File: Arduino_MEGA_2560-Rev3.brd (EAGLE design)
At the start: 111.3 x 99 mm, 32 parts

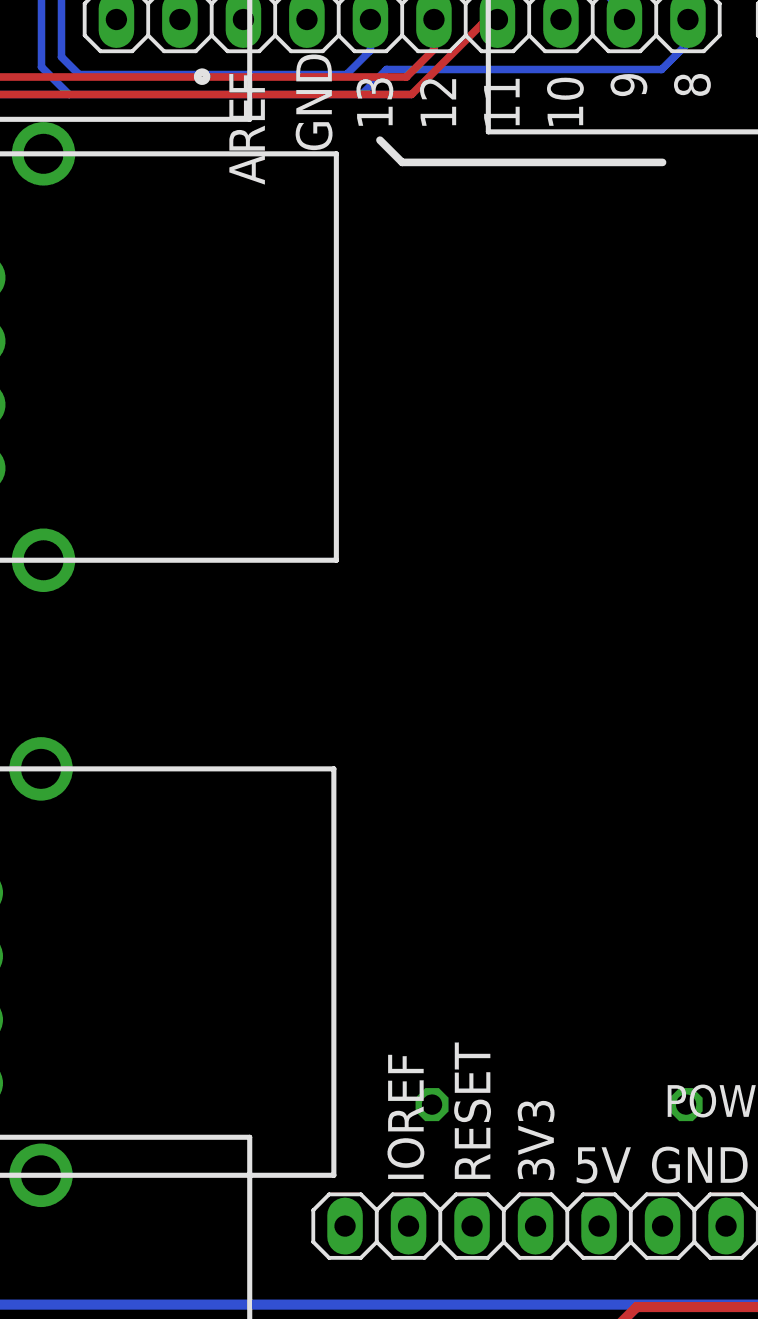
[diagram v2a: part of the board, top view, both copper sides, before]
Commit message: nuevas resistencias, revisar los pines de entrada salida
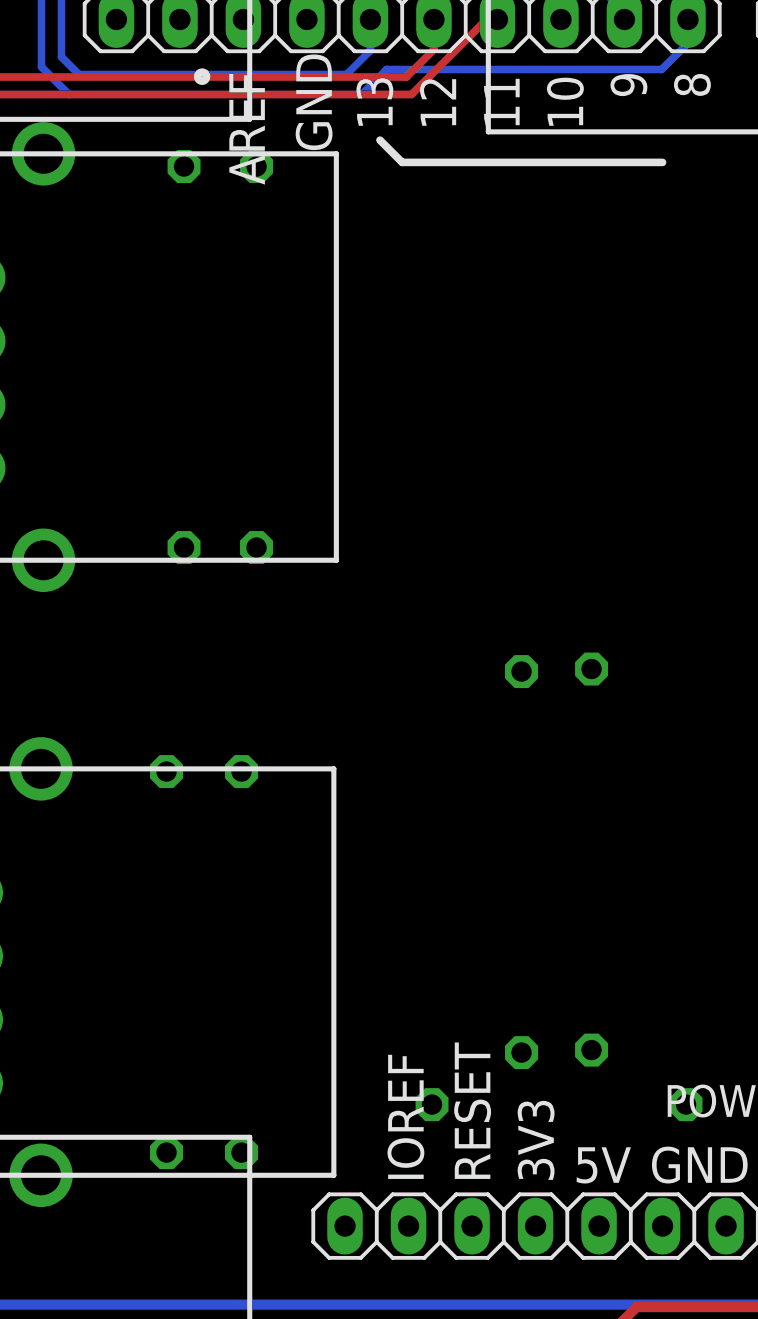
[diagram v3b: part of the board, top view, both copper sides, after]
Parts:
- added R10, R16, R4, R5, R6, R9: (no value), rcl:0207/15
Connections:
- new net N$18: R4.1, U$9.P1, U$9.P2
- new net N$19: R5.2, U$9.P3
- new net N$20: R6.2, U$9.P4
- new net N$26: R16.2, U$1.P1, U$1.P2
- new net N$27: R10.1, U$1.P3
- new net N$28: R9.1, U$1.P4
- net GND: now also R16.1, R4.2; no longer U$1.P1, U$1.P2, U$9.P1, U$9.P2
- net PG0: now also R5.1; no longer U$9.P3
- net PG1: now also R6.1; no longer U$9.P4
- net PL2: now also R10.2; no longer U$1.P3
- net PL3: now also R9.2; no longer U$1.P4
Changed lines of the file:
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@@
 <element name="R15" library="rcl" package="0207/10" value="" x="59.400028125" y="7.200003125" rot="MR180"/>
 <element name="R3" library="rcl" package="0207/10" value="" x="80.90004375" y="6.900003125" rot="MR0"/>
+<element name="R4" library="rcl" package="0207/15" value="" x="37.800021875" y="17.200009375" rot="MR270"/>
+<element name="R5" library="rcl" package="0207/15" value="" x="21.5000125" y="37.300015625" rot="MR270"/>
+<element name="R6" library="rcl" package="0207/15" value="" x="24.400015625" y="37.300021875" rot="MR270"/>
+<element name="R9" library="rcl" package="0207/15" value="" x="23.8000125" y="13.10000625" rot="MR90"/>
+<element name="R10" library="rcl" package="0207/15" value="" x="20.8000125" y="13.10000625" rot="MR90"/>
+<element name="R16" library="rcl" package="0207/15" value="" x="35.000015625" y="17.100009375" rot="MR90"/>
 </elements>
 <signals>
@@
 <contactref element="POWER" pad="6"/>
 <contactref element="POWER" pad="7"/>
-<contactref element="U$1" pad="P1"/>
-<contactref element="U$1" pad="P2"/>
 <contactref element="LED1" pad="C"/>
 <contactref element="LED2" pad="C"/>
-<contactref element="U$9" pad="P1"/>
-<contactref element="U$9" pad="P2"/>
 <contactref element="U$6" pad="P1"/>
 <contactref element="U$6" pad="P2"/>
@@
 <contactref element="R15" pad="1"/>
 <contactref element="R3" pad="2"/>
+<contactref element="R4" pad="2"/>
+<contactref element="R16" pad="1"/>
 <wire x1="88.555" y1="60.68" x2="89.825" y2="63.22" width="0" layer="19" extent="1-1"/>
 <wire x1="64.625" y1="63.52" x2="88.555" y2="60.68" width="0" layer="19" extent="1-1"/>
@@
 <wire x1="37.355" y1="60.48" x2="38.625" y2="63.02" width="0" layer="19" extent="1-1"/>
 <wire x1="26.416" y1="50.8" x2="37.355" y2="60.48" width="0" layer="19" extent="1-1"/>
-<wire x1="13.42" y1="32.855" x2="26.416" y2="50.8" width="0" layer="19" extent="1-1"/>
-<wire x1="10.88" y1="34.125" x2="13.42" y2="32.855" width="0" layer="19" extent="1-1"/>
-<wire x1="3.3" y1="53.72" x2="10.88" y2="34.125" width="0" layer="19" extent="1-1"/>
-<wire x1="10.78" y1="9.525" x2="13.42" y2="32.855" width="0" layer="19" extent="1-1"/>
-<wire x1="13.32" y1="8.255" x2="10.78" y2="9.525" width="0" layer="19" extent="1-1"/>
-<wire x1="40.64" y1="2.54" x2="13.32" y2="8.255" width="0" layer="19" extent="1-1"/>
-<wire x1="43.18" y1="2.54" x2="40.64" y2="2.54" width="0" layer="19" extent="1-1"/>
-<wire x1="41.58" y1="7.4" x2="40.64" y2="2.54" width="0" layer="19" extent="1-1"/>
-<wire x1="54.320028125" y1="7.200003125" x2="43.18" y2="2.54" width="0" layer="19" extent="1-1"/>
-<wire x1="75.82004375" y1="6.900003125" x2="54.320028125" y2="7.200003125" width="0" layer="19" extent="1-1"/>
+<wire x1="3.3" y1="53.72" x2="26.416" y2="50.8" width="0" layer="19" extent="1-1"/>
+<wire x1="75.82004375" y1="6.900003125" x2="71.7" y2="37.45" width="0" layer="19" extent="1-1"/>
 <wire x1="93.98" y1="7.62" x2="75.82004375" y2="6.900003125" width="0" layer="19" extent="1-1"/>
 <wire x1="96.52" y1="7.62" x2="93.98" y2="7.62" width="0" layer="19" extent="1-1"/>
+<wire x1="54.320028125" y1="7.200003125" x2="75.82004375" y2="6.900003125" width="0" layer="19" extent="1-1"/>
+<wire x1="43.18" y1="2.54" x2="54.320028125" y2="7.200003125" width="0" layer="19" extent="1-1"/>
+<wire x1="40.64" y1="2.54" x2="43.18" y2="2.54" width="0" layer="19" extent="1-1"/>
+<wire x1="41.58" y1="7.4" x2="40.64" y2="2.54" width="0" layer="19" extent="1-1"/>
+<wire x1="37.800021875" y1="9.580009375" x2="41.58" y2="7.4" width="0" layer="19" extent="1-1"/>
+<wire x1="35.000015625" y1="9.480009375" x2="37.800021875" y2="9.580009375" width="0" layer="19" extent="1-1"/>
 </signal>
 <signal name="AREF">
@@
 <signal name="PG0">
 <contactref element="XIO" pad="22"/>
-<contactref element="U$9" pad="P3"/>
-<wire x1="13.42" y1="35.395" x2="96.52" y2="25.4" width="0" layer="19" extent="1-1"/>
+<contactref element="R5" pad="1"/>
+<wire x1="21.5000125" y1="44.920015625" x2="96.52" y2="25.4" width="0" layer="19" extent="1-1"/>
 </signal>
 <signal name="PG1">
 <contactref element="XIO" pad="21"/>
-<contactref element="U$9" pad="P4"/>
-<wire x1="10.88" y1="36.665" x2="93.98" y2="25.4" width="0" layer="19" extent="1-1"/>
+<contactref element="R6" pad="1"/>
+<wire x1="24.400015625" y1="44.920021875" x2="93.98" y2="25.4" width="0" layer="19" extent="1-1"/>
 </signal>
 <signal name="PG2">
@@
 <signal name="PL2">
 <contactref element="XIO" pad="28"/>
-<contactref element="U$1" pad="P3"/>
-<wire x1="13.32" y1="10.795" x2="96.52" y2="17.78" width="0" layer="19" extent="1-1"/>
+<contactref element="R10" pad="2"/>
+<wire x1="20.8000125" y1="20.72000625" x2="96.52" y2="17.78" width="0" layer="19" extent="1-1"/>
 </signal>
 <signal name="PL3">
 <contactref element="XIO" pad="27"/>
-<contactref element="U$1" pad="P4"/>
-<wire x1="10.78" y1="12.065" x2="93.98" y2="17.78" width="0" layer="19" extent="1-1"/>
+<contactref element="R9" pad="2"/>
+<wire x1="23.8000125" y1="20.72000625" x2="93.98" y2="17.78" width="0" layer="19" extent="1-1"/>
 </signal>
 <signal name="PL4">
@@
 <wire x1="93.475" y1="-11.319996875" x2="94.745" y2="-8.779996875" width="0" layer="19" extent="1-1"/>
 </signal>
+<signal name="N$18" class="2">
+<contactref element="U$9" pad="P1"/>
+<contactref element="U$9" pad="P2"/>
+<contactref element="R4" pad="1"/>
+<wire x1="13.42" y1="32.855" x2="37.800021875" y2="24.820009375" width="0" layer="19" extent="1-1"/>
+<wire x1="10.88" y1="34.125" x2="13.42" y2="32.855" width="0" layer="19" extent="1-1"/>
+</signal>
+<signal name="N$19">
+<contactref element="U$9" pad="P3"/>
+<contactref element="R5" pad="2"/>
+<wire x1="13.42" y1="35.395" x2="21.5000125" y2="29.680015625" width="0" layer="19" extent="1-1"/>
+</signal>
+<signal name="N$20">
+<contactref element="U$9" pad="P4"/>
+<contactref element="R6" pad="2"/>
+<wire x1="10.88" y1="36.665" x2="24.400015625" y2="29.680021875" width="0" layer="19" extent="1-1"/>
+</signal>
+<signal name="N$26" class="2">
+<contactref element="U$1" pad="P1"/>
+<contactref element="U$1" pad="P2"/>
+<contactref element="R16" pad="2"/>
+<wire x1="13.32" y1="8.255" x2="35.000015625" y2="24.720009375" width="0" layer="19" extent="1-1"/>
+<wire x1="10.78" y1="9.525" x2="13.32" y2="8.255" width="0" layer="19" extent="1-1"/>
+</signal>
+<signal name="N$27">
+<contactref element="U$1" pad="P3"/>
+<contactref element="R10" pad="1"/>
+<wire x1="13.32" y1="10.795" x2="20.8000125" y2="5.48000625" width="0" layer="19" extent="1-1"/>
+</signal>
+<signal name="N$28">
+<contactref element="U$1" pad="P4"/>
+<contactref element="R9" pad="1"/>
+<wire x1="10.78" y1="12.065" x2="23.8000125" y2="5.48000625" width="0" layer="19" extent="1-1"/>
+</signal>
 </signals>

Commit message: Version 0.1 - Faltan planos de tierra
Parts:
- added R17, R18, R22, R23, R24, R26, R27, R28, R29: (no value), rcl:0207/15
- moved LED2 15.8 mm to (58.2, 30.9)
- moved R2 15.8 mm to (54.9, 31.0)
- moved LED1 15.8 mm to (48.0, 31.0)
- moved R1 15.6 mm to (51.4, 31.1), turned to 270 degrees
- moved R15 2.62 mm to (57.6, 9.10)
- moved R3 2.16 mm to (80.4, 9.00), turned to 180 degrees
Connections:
- removed net N$10: ADCH.3, R7.2
- removed net N$21: ADCH.4, R8.2
- removed net N$22: ADCH.5, U$3.P8
- removed net N$23: ADCH.6, U$3.P7
- removed net N$24: ADCH.7, U$3.P6
- removed net N$25: ADCH.8, U$3.P5
- new net N$29: R17.1, U$6.P1, U$6.P2
- new net N$32: R22.1, U$6.P4
- new net N$33: R18.1, U$6.P3
- new net N$34: R24.1, U$5.P1, U$5.P2
- new net N$35: R23.1, U$4.P1, U$4.P2
- new net N$40: R28.1, U$5.P4
- new net N$41: R29.1, U$5.P3
- new net N$42: R26.2, U$4.P4
- new net N$43: R27.1, U$4.P3
- net GND: now also R17.2, R23.2, R24.2; no longer U$4.P1, U$4.P2, U$5.P1, U$5.P2, U$6.P1, U$6.P2
- net PA0: now also R7.2
- net PA1: now also R8.2
- net PA2: now also U$3.P6
- net PA3: now also U$3.P5
- net PA4: now also U$3.P8
- net PA5: now also U$3.P7
- net PA6: now also R26.1
- net PA7: now also R27.2
- net PC0: now also U$6.P5
- net PC1: now also U$6.P6
- net PC2: now also R18.2
- net PC3: now also R22.2
- net PC4: now also U$4.P7
- net PC5: now also U$4.P8
- net PC6: now also U$4.P5
- net PC7: now also U$4.P6
- net PD7: now also U$6.P8
- net PE3: now also U$5.P5
- net PE4: now also U$5.P8
- net PE5: now also U$5.P7
- net PG2: now also U$6.P7
- net PG5: now also U$5.P6
- net PH3: now also R28.2
- net PH4: now also R29.2
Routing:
- net PL4: track 0.00 -> 121.4 mm
- net PL5: track 0.00 -> 106.3 mm
- net PL6: track 0.00 -> 95.0 mm
- net PL7: track 0.00 -> 94.1 mm
- net PG0: track 0.00 -> 90.2 mm
- net PB2: track 0.00 -> 87.3 mm, vias 0 -> 1
- net PB3: track 0.00 -> 85.8 mm, vias 0 -> 1
- net PL0: track 0.00 -> 84.4 mm
- net PG1: track 0.00 -> 83.7 mm
- net PL1: track 0.00 -> 83.5 mm
- net PL2: track 0.00 -> 78.0 mm
- net PA2: track 0.00 -> 75.3 mm, vias 0 -> 1
- net PA4: track 0.00 -> 74.4 mm, vias 0 -> 3
- net PL3: track 0.00 -> 71.4 mm
- net PA1: track 0.00 -> 67.9 mm
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
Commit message: Terminada la version 1.0
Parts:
- added COMMUNICATION1: 8x1F-H8.5, SmartPrj:1X08
- added JP1: (no value), pinhead:1X06
- moved R17 37.7 mm to (80.3, 65.6), turned to 270 degrees
- moved LED2 0.10 mm to (58.2, 31.0)
- turned R3 to 0 degrees
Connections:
- new net N$10: ADCH.3, JP1.1
- new net N$21: ADCH.4, JP1.2
- new net N$22: ADCH.5, JP1.3
- new net N$23: ADCH.6, JP1.4
- new net N$24: ADCH.7, JP1.5
- new net N$25: ADCH.8, JP1.6
- net RXD1: now also COMMUNICATION1.3
- net RXD2: now also COMMUNICATION1.5
- net RXD3: now also COMMUNICATION1.7
- net SCL: now also COMMUNICATION1.1
- net SDA: now also COMMUNICATION1.2
- net TXD1: now also COMMUNICATION1.4
- net TXD2: now also COMMUNICATION1.6
- net TXD3: now also COMMUNICATION1.8
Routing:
- net +5V: track 0.00 -> 55.9 mm
- net N$26: track 0.00 -> 44.1 mm
- net N$46: track 0.00 -> 42.8 mm
- net N$35: track 0.00 -> 42.1 mm
- net N$17: track 0.00 -> 37.7 mm
- net N$18: track 0.00 -> 34.5 mm
- net N$16: track 0.00 -> 22.0 mm
- net N$29: track 0.00 -> 20.9 mm
- net N$34: track 0.00 -> 19.4 mm
- net N$6: track 0.00 -> 12.4 mm
- net TXD3: track 0.00 -> 4.60 mm
- net RXD3: track 0.00 -> 4.36 mm
- net TXD1: track 0.00 -> 4.36 mm
- net SDA: track 0.00 -> 4.36 mm
- net SCL: track 0.00 -> 4.36 mm
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- added copper zone on layer 1, net GND
- added copper zone on layer 16, net GND
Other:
- board text added: "02/09/2014"
- board text added: "Digital I/O Shield"
- board text added: "KRADAC 2014"
- board text added: "WWW.KRADAC.COM"
- board text added: "v 1.0"
